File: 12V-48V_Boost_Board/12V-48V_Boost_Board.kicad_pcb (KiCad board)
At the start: 2 copper layers, 65 x 109.7 mm, 35 parts, among them J1 12V Input, J2 Input Current Sensing, J3 Output Current Sensing, J4 48V Output, J5 Output Measuring, Q1 FDWS86068-F085

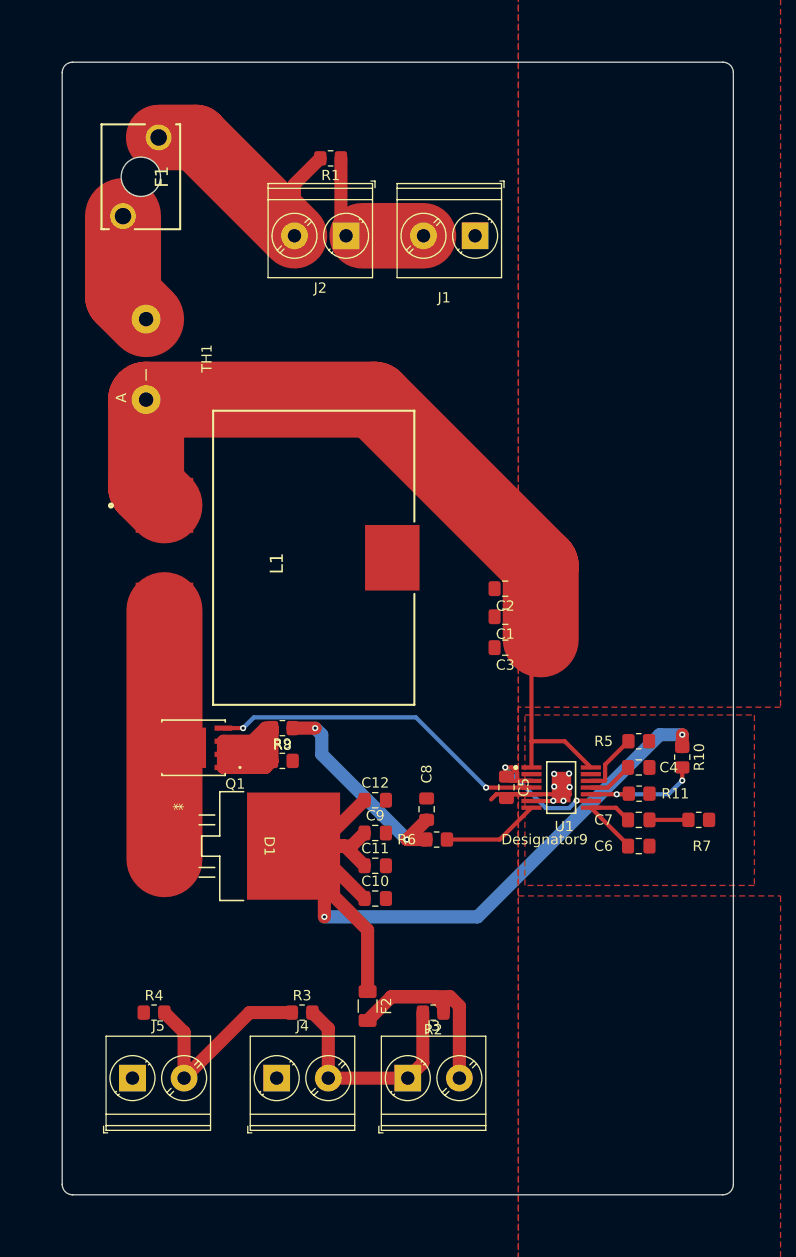
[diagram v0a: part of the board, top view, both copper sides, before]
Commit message: Added mounting holes
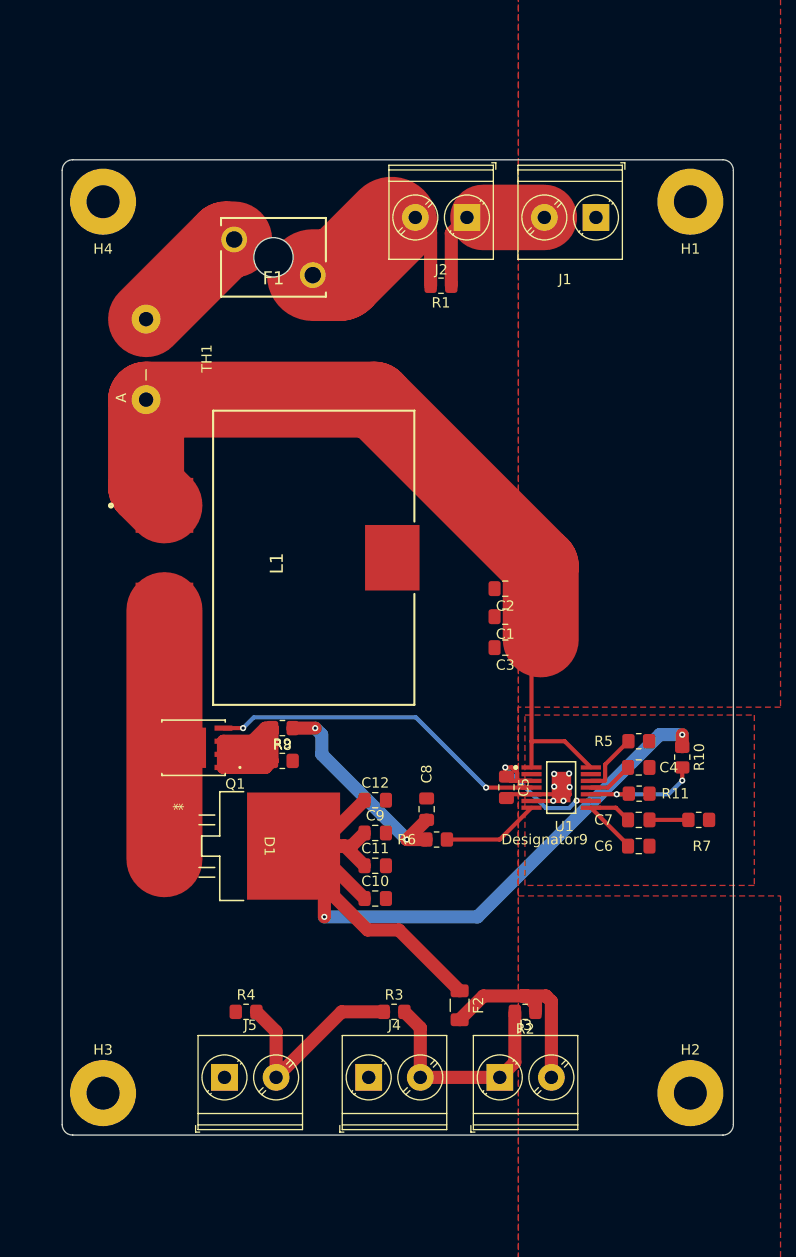
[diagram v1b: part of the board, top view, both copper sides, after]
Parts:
- added H1: MountingHole_Pad, MountingHole:MountingHole_3.2mm_M3_Pad, F.Cu at (167.6, 62.0)
- added H2: MountingHole_Pad, MountingHole:MountingHole_3.2mm_M3_Pad, F.Cu at (167.6, 148.3)
- added H3: MountingHole_Pad, MountingHole:MountingHole_3.2mm_M3_Pad, F.Cu at (110.7, 148.3)
- added H4: MountingHole_Pad, MountingHole:MountingHole_3.2mm_M3_Pad, F.Cu at (110.7, 62.0)
- moved F1 20.0 mm to (131.1, 69.1), turned to 180 degrees
- moved R1 16.3 mm to (143.5, 70.1)
- moved J1 11.8 mm to (158.5, 63.5)
- moved J2 11.8 mm to (146.0, 63.5)
- moved F2 8.91 mm to (145.3, 139.8)
- moved R2 8.91 mm to (151.6, 140.5)
- moved J4 8.91 mm to (136.5, 146.8)
- moved J5 8.91 mm to (122.5, 146.8)
- moved R4 8.91 mm to (124.6, 140.5)
- moved J3 8.91 mm to (149.2, 146.8)
- moved R3 8.91 mm to (138.9, 140.5)
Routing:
- net Net-(J2-Pin_2): track 25.6 -> 17.0 mm
- net /Boost_Board_Chip/48V_OUTPUT: track 91.7 -> 97.1 mm
- net GND: track 20.6 -> 16.5 mm
- net Net-(J3-Pin_2): track 23.3 -> 19.7 mm
- net Net-(F1-Pad2): track 10.9 -> 11.7 mm
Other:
- board size 65 x 109.7 mm -> 65 x 94.5 mm

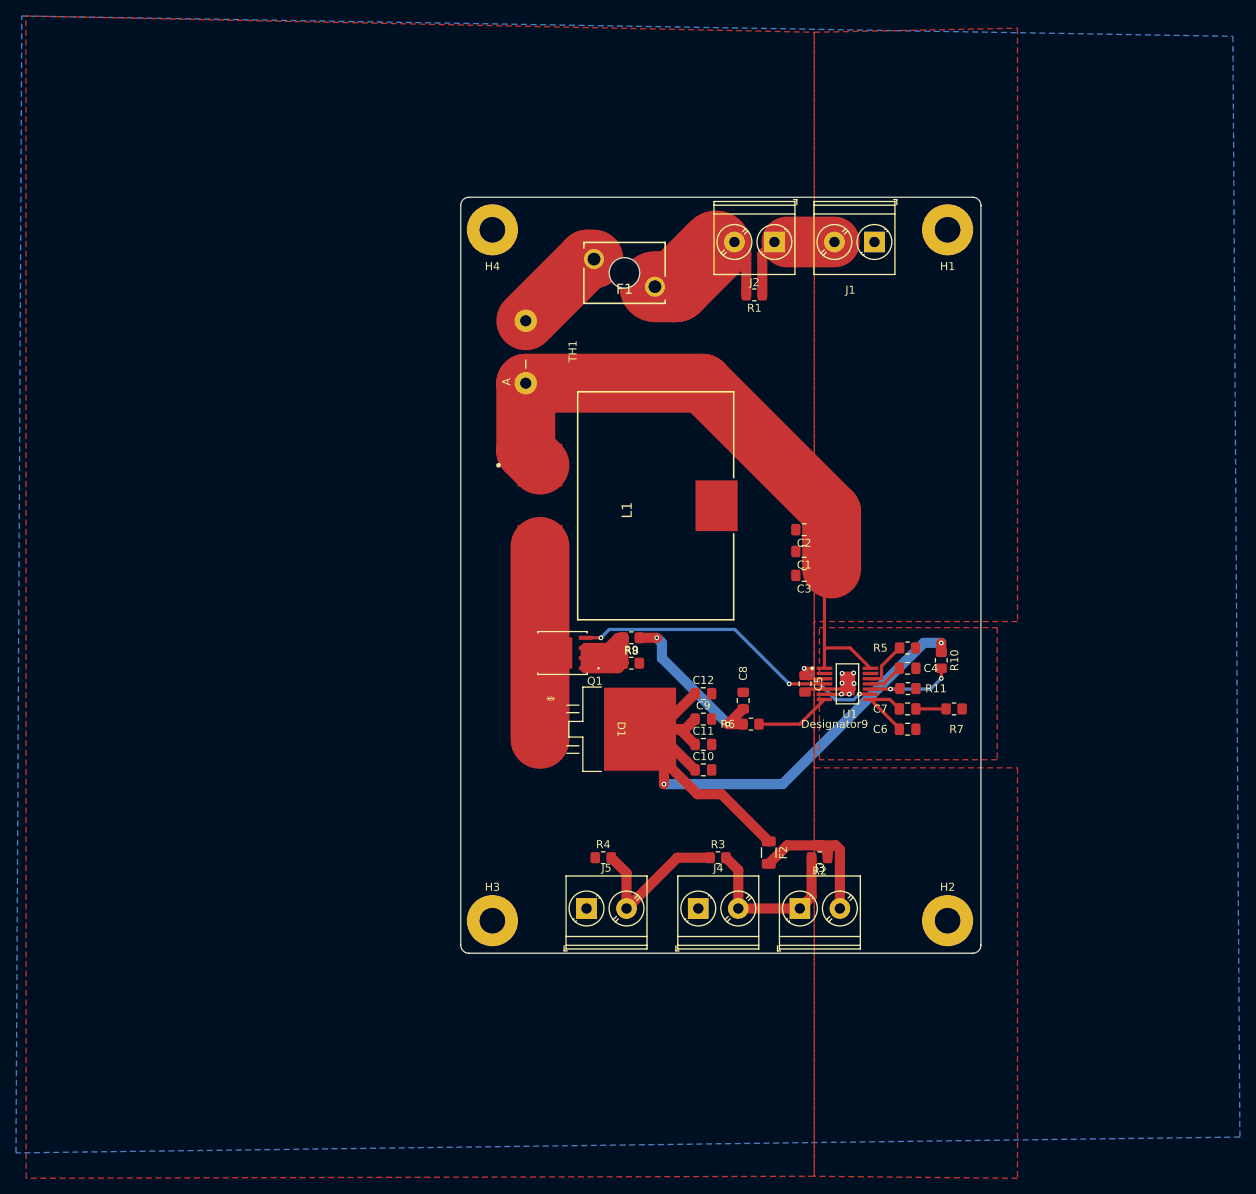
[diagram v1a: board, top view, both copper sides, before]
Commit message: Changed layout to make it more compact, changed output and input cap sizes
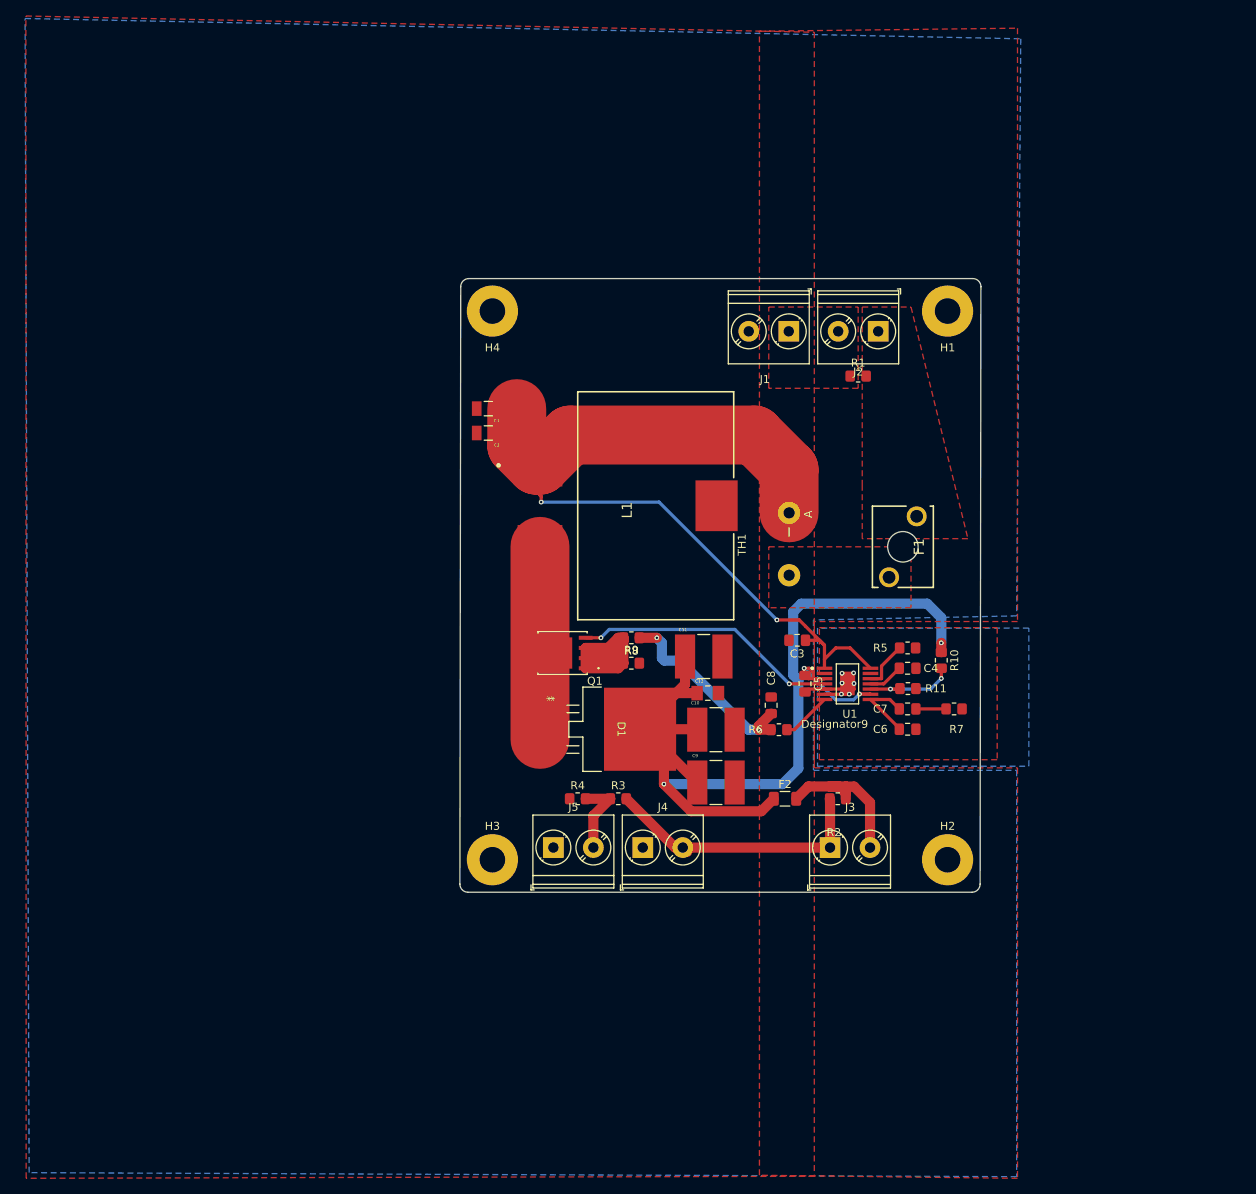
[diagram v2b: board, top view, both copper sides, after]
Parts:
- C1, C2: footprint Capacitor_SMD:C_0805_2012Metric_Pad1.18x1.45mm_HandSolder -> 12/48 boost:GRM31CR71H475KA12L
- C10, C11, C9: footprint Capacitor_SMD:C_0805_2012Metric_Pad1.18x1.45mm_HandSolder -> 12/48 boost:CAPC6050X550N
- C12: footprint Capacitor_SMD:C_0805_2012Metric_Pad1.18x1.45mm_HandSolder -> 12/48 boost:CAPC3216X180N
- moved TH1 45.8 mm to (147.8, 105.2), turned to 90 degrees
- moved F1 43.5 mm to (163.8, 97.8), turned to -90 degrees
- moved C1 43.3 mm to (110.2, 84.3)
- moved C2 41.3 mm to (110.2, 87.4)
- moved J2 17.1 mm to (159.0, 74.7)
- moved R1 16.5 mm to (156.5, 80.3), turned to 0 degrees
- moved J1 15.5 mm to (147.8, 74.7)
- moved R3 14.5 mm to (126.5, 133.1)
- moved C11 11.0 mm to (137.2, 115.3)
- moved J4 10.3 mm to (129.5, 139.2)
- moved H1 10.2 mm to (167.6, 72.1)
- moved H4 10.2 mm to (110.7, 72.1)
- moved J5 8.67 mm to (118.4, 139.2)
- moved J3 8.49 mm to (152.9, 139.2)
- moved C3 8.15 mm to (148.8, 113.3)
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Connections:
- F1 pad 1: Net-(J2-Pin_2) -> Net-(J2-Pin_1)
- J1 pad 1: GND -> Net-(J1-Pin_1)
- J1 pad 2: Net-(J1-Pin_2) -> GND
- J2 pad 1: Net-(J1-Pin_2) -> Net-(J2-Pin_1)
- J2 pad 2: Net-(J2-Pin_2) -> Net-(J1-Pin_1)
- R1 pad 1: Net-(J1-Pin_2) -> Net-(J1-Pin_1)
- R1 pad 2: Net-(J2-Pin_2) -> Net-(J2-Pin_1)
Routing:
- net /Boost_Board_Chip/12V_INPUT: track 81.8 -> 109.2 mm, vias 0 -> 2
- net /Boost_Board_Chip/48V_OUTPUT: track 97.1 -> 123.4 mm
- net Net-(J2-Pin_2): track 17.0 -> 0.00 mm
- net Net-(J3-Pin_1): track 21.6 -> 34.9 mm
- net Net-(J1-Pin_2): track 13.2 -> 0.00 mm
- net Net-(F1-Pad2): track 11.7 -> 0.00 mm
- net Net-(J5-Pin_2): track 20.2 -> 10.1 mm
- net Net-(C8-Pad1): track 21.2 -> 25.0 mm
- net Net-(U1-CS): track 9.47 -> 6.26 mm
- added copper zone on F.Cu, net Net-(F1-Pad2)
- added copper zone on F.Cu, net Net-(J1-Pin_1)
- added copper zone on F.Cu, net Net-(J2-Pin_1)
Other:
- board size 65 x 94.5 mm -> 65.1 x 76.7 mm

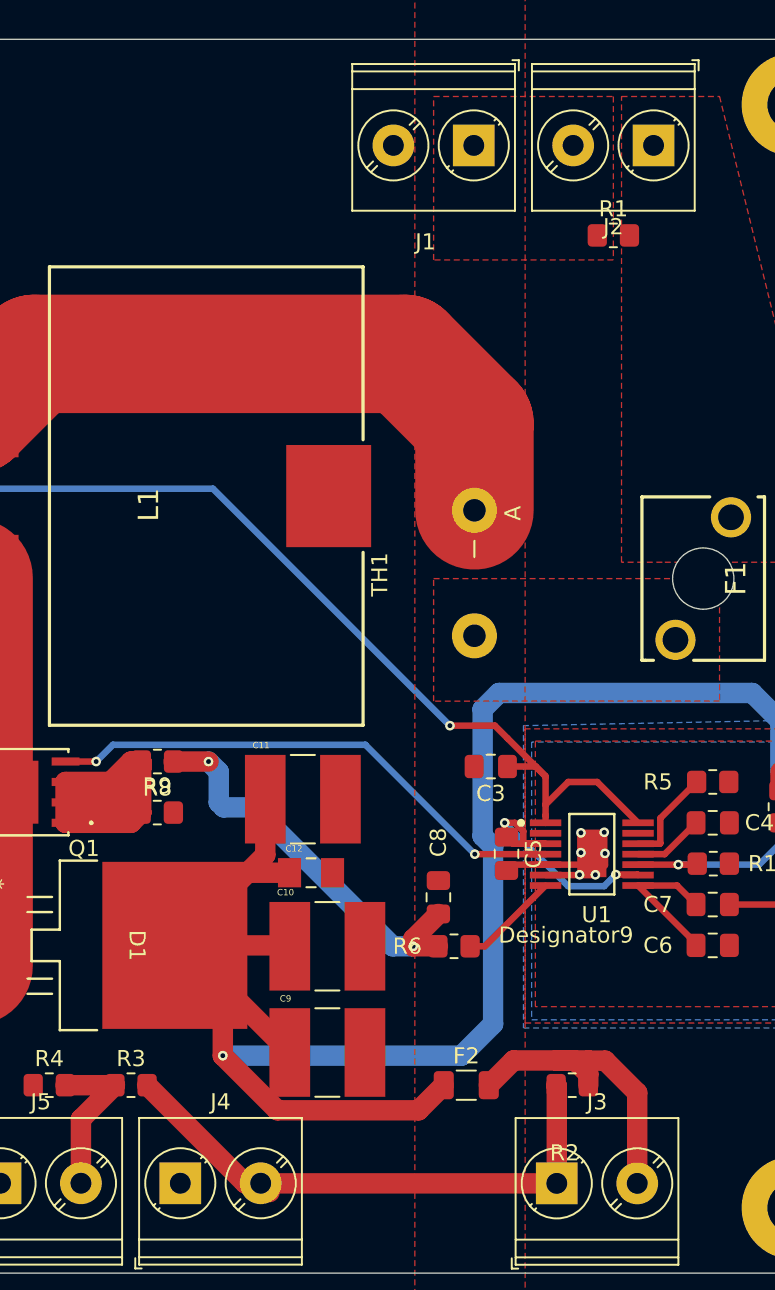
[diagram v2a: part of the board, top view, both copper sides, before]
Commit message: Made the two resistors bigger, will implement other changes after some discussion
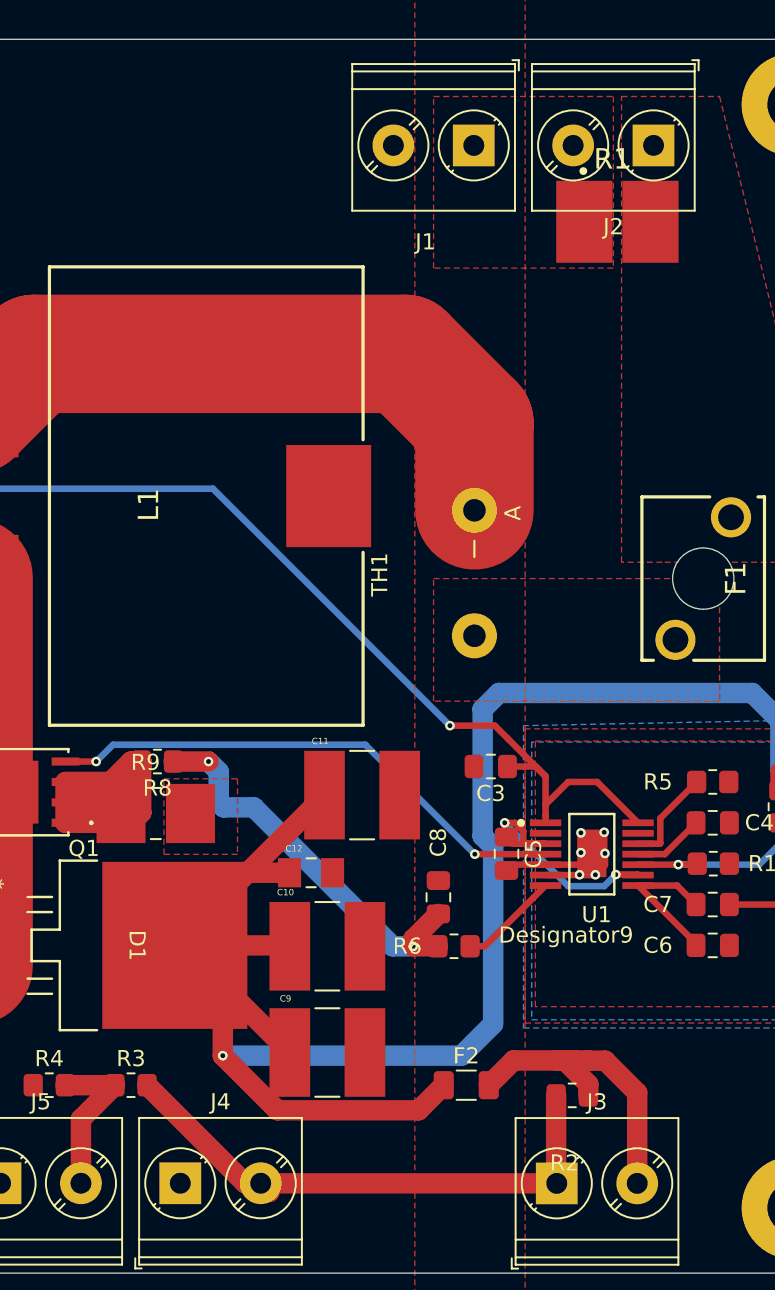
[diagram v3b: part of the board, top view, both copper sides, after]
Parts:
- R1: footprint Resistor_SMD:R_0805_2012Metric_Pad1.20x1.40mm_HandSolder -> 12/48 boost:WSHM28181L000FEA
- R9: footprint Resistor_SMD:R_0805_2012Metric_Pad1.20x1.40mm_HandSolder -> 12/48 boost:RES_WSL25124L000FEB
- moved C11 3.69 mm to (140.8, 115.1)
- moved R1 0.88 mm to (156.7, 79.4)
- moved R2 0.63 mm to (153.9, 133.7)
- moved R9 0.11 mm to (128.0, 116.2)
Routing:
- net /Boost_Board_Chip/48V_OUTPUT: track 123.4 -> 125.2 mm
- net Net-(J3-Pin_2): track 19.4 -> 20.8 mm
- net Net-(J3-Pin_1): track 34.9 -> 34.3 mm
